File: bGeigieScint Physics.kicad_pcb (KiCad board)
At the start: 4 copper layers, 33 x 27.9 mm, 7 parts, among them U1 TMP116xxDRV, U2 AT24CS01-STUM, U3 AFBR-S4N44P014M

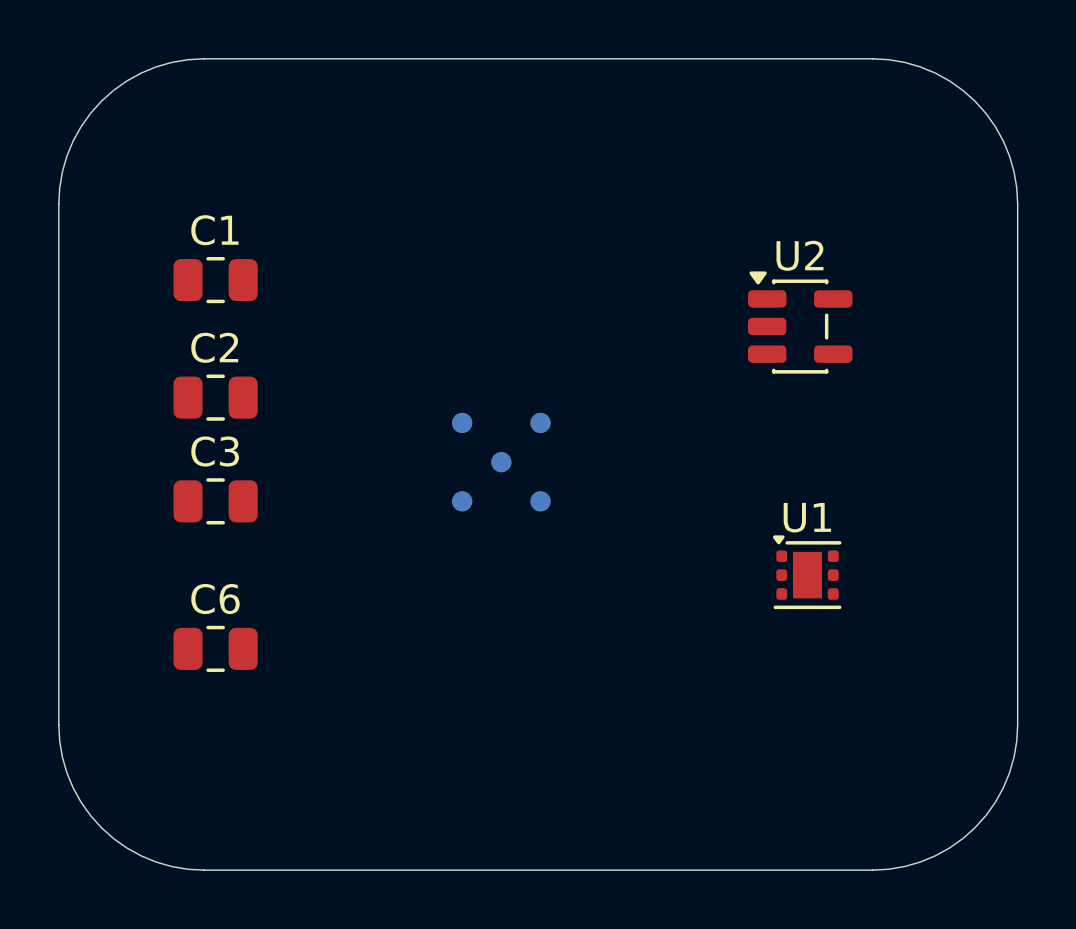
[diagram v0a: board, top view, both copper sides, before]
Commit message: feat: Add new KiCad component libraries and update schematic/PCB.
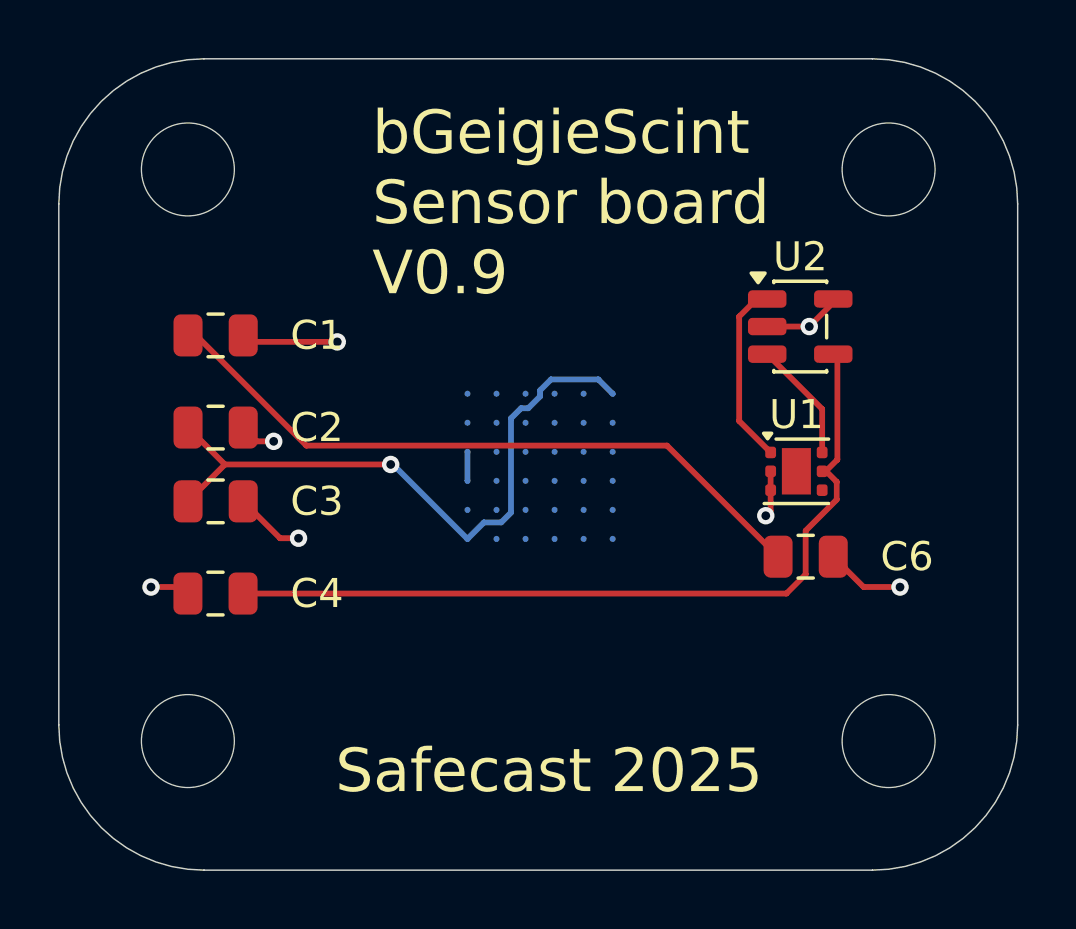
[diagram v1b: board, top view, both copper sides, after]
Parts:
- removed U3: AFBR-S4N44P014M, bGeigieScint:AFBRS4N44P014M
- added C4: 100nF, Capacitor_SMD:C_0805_2012Metric, F.Cu at (136.2, 97.2)
- added H1: MountingHole, MountingHole:MountingHole_3.2mm_M3, F.Cu at (135.3, 82.5)
- added H2: MountingHole, MountingHole:MountingHole_3.2mm_M3, F.Cu at (159.4, 82.5)
- added H3: MountingHole, MountingHole:MountingHole_3.2mm_M3, F.Cu at (159.4, 102.2)
- added H4: MountingHole, MountingHole:MountingHole_3.2mm_M3, F.Cu at (135.3, 102.2)
- added IC1: MICROFJ-60035-TSV-TR, bGeigieScint:BGA36C100P6X6_613X613X67, B.Cu at (147.4, 92.8)
- moved C6 20.6 mm to (156.5, 95.9)
- moved U1 3.60 mm to (156.2, 92.9)
- moved C1 1.91 mm to (136.2, 88.3)
- moved C2 1.03 mm to (136.2, 91.4)
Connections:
- net /GND renamed GND
- net /SiPM_K renamed Net-(IC1-CATHODE_1)
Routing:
- net /3V3: track 0.00 -> 28.3 mm
- net Net-(C1-Pad1): track 0.00 -> 23.5 mm
- net Net-(IC1-CATHODE_1): track 0.00 -> 22.5 mm, vias 0 -> 1
- net GND: track 0.00 -> 15.4 mm, vias 0 -> 7
- net /PA17: track 0.00 -> 6.35 mm
- net /PA16: track 0.00 -> 4.17 mm
- net /SiPM_A: track 0.00 -> 1.00 mm
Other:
- board text added: "Safecast 2025"
- board text added: "bGeigieScint Sensor board V0.9"

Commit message: feat: Assign footprints to schematic components, add a new net, and place pin headers on the PCB while adjusting a mounting hole.
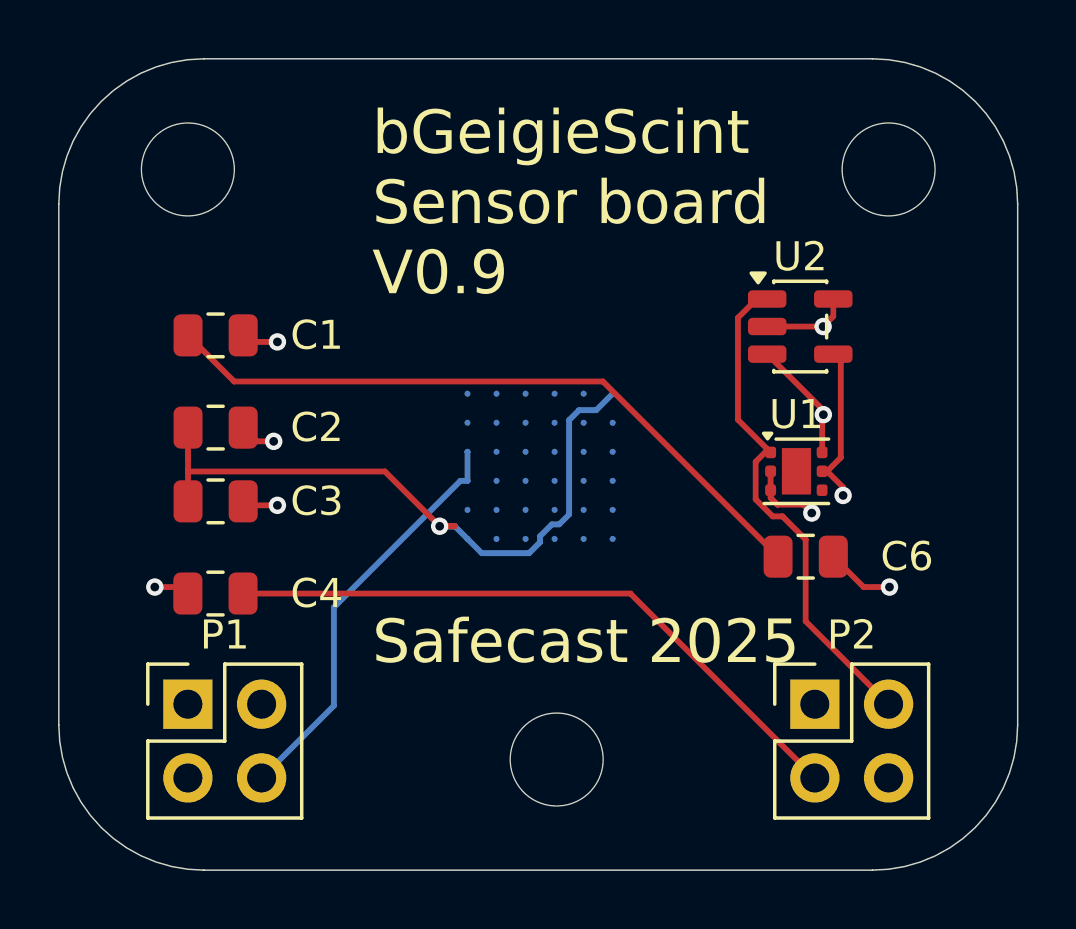
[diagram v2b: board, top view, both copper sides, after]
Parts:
- removed H3: MountingHole, MountingHole:MountingHole_3.2mm_M3
- added P1: Header-Male-2.54_2x2, Connector_PinHeader_2.54mm:PinHeader_2x02_P2.54mm_Vertical, F.Cu at (135.3, 101.0)
- added P2: Header-Male-2.54_2x2, Connector_PinHeader_2.54mm:PinHeader_2x02_P2.54mm_Vertical, F.Cu at (156.8, 101.0)
- moved H4 12.7 mm to (148.0, 102.9)
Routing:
- net /PA16: track 4.17 -> 18.6 mm, vias 0 -> 1
- net /SiPM_A: track 1.00 -> 14.3 mm
- net /PA17: track 6.35 -> 17.4 mm
- net /3V3: track 28.3 -> 38.2 mm, vias 0 -> 1
- net GND: track 15.4 -> 12.9 mm
- net Net-(IC1-CATHODE_1): track 22.5 -> 24.7 mm

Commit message: Refactor code structure for improved readability and maintainability
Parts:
- added R1: 100Ω, Resistor_SMD:R_0805_2012Metric, F.Cu at (141.0, 88.6)
- added R3: 100Ω, Resistor_SMD:R_0805_2012Metric, F.Cu at (144.6, 88.6)
- added R4: 10kΩ, Resistor_SMD:R_0805_2012Metric, F.Cu at (148.2, 88.6)
- added R5: 10kΩ, Resistor_SMD:R_0805_2012Metric, F.Cu at (151.8, 88.6)
- P1, P2: footprint Connector_PinHeader_2.54mm:PinHeader_2x02_P2.54mm_Vertical -> Connector_PinHeader_2.54mm:PinHeader_2x02_P2.54mm_Vertical_SMD
- moved P1 1.82 mm to (136.6, 102.2)
- moved P2 1.43 mm to (157.5, 102.2)
- moved C6 0.71 mm to (156.8, 96.5)
- moved U2 0.62 mm to (156.3, 88.6)
- moved C2 0.21 mm to (136.2, 91.2)
- moved C3 0.21 mm to (136.2, 94.2)
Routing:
- net /Vbias: track 0.00 -> 23.0 mm, vias 0 -> 2
- net /3V3: track 38.2 -> 52.4 mm, vias 1 -> 0
- net Net-(C1-Pad1): track 23.5 -> 37.0 mm, vias 0 -> 2
- net /PA17: track 17.4 -> 29.4 mm
- net Net-(IC1-CATHODE_1): track 24.7 -> 34.6 mm
- net GND: track 12.9 -> 21.8 mm, vias 7 -> 11
- net /PA16: track 18.6 -> 24.3 mm, vias 1 -> 2
- net /SiPM_A: track 14.3 -> 14.9 mm, vias 0 -> 1
- added copper zone on B.Cu, net GND
- added copper zone on F.Cu, net GND
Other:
- board text added: "bGeigieScint Sensor-board V0.9"
- board text removed: "bGeigieScint Sensor board V0.9"
